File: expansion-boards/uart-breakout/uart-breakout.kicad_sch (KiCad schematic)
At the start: 78 parts, among them J1 Conn_01x06, J2 Conn_01x06, J3 Conn_02x12_Odd_Even, J4 Conn_01x06, J5 Conn_01x06, J6 Conn_01x06, J7 Conn_01x06, J8 Conn_01x06, J9 Conn_01x06, U1 74HC02, U2 74HC00, U3 16C2552_PLCC, U4 DS1813, U5 74LS573, U6 16C2552_PLCC, U7 16C2552_PLCC, U8 16C2552_PLCC, X1 14.7456M

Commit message: [exp-uart] Pre-ERC schematic complete
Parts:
- removed C1: 150u, Capacitor_THT:C_Radial_D8.0mm_H7.0mm_P3.50mm, symbol Device:C_Polarized
- removed R11, R13, R14, R15, R16, R17, R19, R2, R20, R21, R24, R25, R26, R27, R28, R29, R3, R30, R31, R34, R35, R36, R37, R38, R39, R4, R40, R41, R5, R6, R8, R9: 1k, Resistor_THT:R_Axial_DIN0207_L6.3mm_D2.5mm_P7.62mm_Horizontal, symbol Device:R
- removed U1: 74HC02, Package_DIP:DIP-14_W7.62mm, symbol 74xx:74HC02
- removed U5: 74LS573, Package_DIP:DIP-20_W7.62mm, symbol 74xx:74LS573
- added C1, C10, C2, C3, C4, C5, C6, C7, C9: 0.1u, Capacitor_THT:C_Disc_D4.3mm_W1.9mm_P5.00mm, symbol Device:C
- added J10: Conn_01x07, symbol Connector_Generic:Conn_01x07
- added J11: Conn_01x01, symbol Connector_Generic:Conn_01x01
- added J12: Conn_02x12_Odd_Even, Connector_PinSocket_2.54mm:PinSocket_2x12_P2.54mm_Vertical, symbol Connector_Generic:Conn_02x12_Odd_Even
- added R10, R44, R45, R46: 10k, Resistor_THT:R_Axial_DIN0207_L6.3mm_D2.5mm_P7.62mm_Horizontal, symbol Device:R
- added RN1: 1k, Resistor_THT:R_Array_SIP9, symbol Device:R_Network08
- added RN2, RN3, RN4, RN5: 10k, Resistor_THT:R_Array_SIP9, symbol Device:R_Network08
- added SW1: SW_Push, Button_Switch_THT:SW_PUSH_6mm, symbol Switch:SW_Push
- added U1: 74HC04, symbol 74xx:74HC04
- added U10: 74LVC1G07, Package_TO_SOT_SMD:SOT-353_SC-70-5_Handsoldering, symbol 74xGxx:74LVC1G07
- added unit 5 of U2
- added unit 3 of U2
- added U5: 74ACT563, symbol Custom:74ACT563
- added U9: 74HCT164, symbol 74xx:74HCT164
- R18: value 1k -> 10k
- U4: footprint (none) -> Package_TO_SOT_THT:TO-92L_Wide
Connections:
- net A0: now also J12.6 (Pin_6)
- net A1: now also J12.4 (Pin_4)
- net A2: now also J12.5 (Pin_5)
- net A3: now also J12.3 (Pin_3)
- net AUXCSB0: now also U5.1 (OE)
- net AUXCSB1: now also U1.5, U9.2 (DSB)
- net AUXCSB2: now also J12.11 (Pin_11)
- net AUXCSB3: now also J12.13 (Pin_13)
- net B4: now also J12.7 (Pin_7), RN1.5 (R4), U5.16 (Q3)
- net B5: now also RN1.4 (R3), U5.17 (Q2)
- net B6: now also RN1.3 (R2), U5.18 (Q1)
- net B7: now also RN1.2 (R1), U5.19 (Q0)
- net D0: now also J12.8 (Pin_8), U5.9 (D7)
- net D1: now also J12.10 (Pin_10), U5.8 (D6)
- net D2: now also J12.12 (Pin_12), U5.7 (D5)
- net D3: now also J12.14 (Pin_14), U5.6 (D4)
- net D4: now also J12.16 (Pin_16), U5.5 (D3)
- net D5: now also J12.18 (Pin_18), U5.4 (D2)
- net D6: now also J12.20 (Pin_20), U5.3 (D1)
- net D7: now also J12.22 (Pin_22), U5.2 (D0)
- net GND: now also C8.2, C1.2, C10.2, C2.2, C3.2, C4.2, C5.2, C6.2, C7.2, C9.2, J12.23 (Pin_23), J12.24 (Pin_24), R45.2, R46.2, SW1.1, U1.7 (GND), U10.3 (GND), U2.7 (GND), U5.10 (GND), U9.7 (GND); no longer R1.2
- net PHI1: now also U1.2, U5.11 (Load)
- net PHI2: now also U2.2, J12.15 (Pin_15), U1.1, U9.8 (CP)
- net RES: now also U8.21 (RESET), U1.4
- net VDD: now also C8.1, R1.1, C1.1, C10.1, C2.1, C3.1, C4.1, C5.1, C6.1, C7.1, C9.1, J12.1 (Pin_1), R10.1, R44.1, RN1.1 (common), RN2.1 (common), RN3.1 (common), RN4.1 (common), RN5.1 (common), U1.14 (VCC), U10.5 (VCC), U2.14 (VCC), U5.20 (VCC), U9.14 (VCC)
- net /RDB: now also J12.19 (Pin_19)
- net /RDY: now also J12.2 (Pin_2), U10.4
- net /RWB: now also J12.17 (Pin_17)
- net /WRB: now also J12.21 (Pin_21)
- net ~{CD0B}: now also RN2.6 (R5)
- net ~{CD1B}: now also RN2.2 (R1)
- net ~{CD2B}: now also RN3.6 (R5)
- net ~{CD3B}: now also RN3.2 (R1)
- net ~{CD4B}: now also RN4.6 (R5)
- net ~{CD5B}: now also RN4.2 (R1)
- net ~{CD6B}: now also RN5.6 (R5)
- net ~{CD7B}: now also RN5.2 (R1)
- net ~{CS0}: now also RN1.9 (R8), U5.12 (Q7)
- net ~{CS1}: now also RN1.8 (R7), U5.13 (Q6)
- net ~{CS2}: now also RN1.7 (R6), U5.14 (Q5)
- net ~{CS3}: now also RN1.6 (R5), U5.15 (Q4)
- net ~{CTS0B}: now also RN2.7 (R6)
- net ~{CTS1B}: now also RN2.3 (R2)
- net ~{CTS2B}: now also RN3.7 (R6)
- net ~{CTS3B}: now also RN3.3 (R2)
- net ~{CTS4B}: now also RN4.7 (R6)
- net ~{CTS5B}: now also RN4.3 (R2)
- net ~{CTS6B}: now also RN5.7 (R6)
- net ~{CTS7B}: now also RN5.3 (R2)
- net ~{DSR0B}: now also RN2.8 (R7)
- net ~{DSR1B}: now also RN2.4 (R3)
- net ~{DSR2B}: now also RN3.8 (R7)
- net ~{DSR3B}: now also RN3.4 (R3)
- net ~{DSR4B}: now also RN4.8 (R7)
- net ~{DSR5B}: now also RN4.4 (R3)
- net ~{DSR6B}: now also RN5.8 (R7)
- net ~{DSR7B}: now also RN5.4 (R3)
- net ~{RI0B}: now also RN2.9 (R8)
- net ~{RI1B}: now also RN2.5 (R4)
- net ~{RI2B}: now also RN3.9 (R8)
- net ~{RI3B}: now also RN3.5 (R4)
- net ~{RI4B}: now also RN4.9 (R8)
- net ~{RI5B}: now also RN4.5 (R4)
- net ~{RI6B}: now also RN5.9 (R8)
- net ~{RI7B}: now also RN5.5 (R4)
- net at U2.4: now also R18.1
- net at U2.5: now also R46.1
- net at U4.1 (RST): now also R1.2, SW1.2, U1.3
- net at U2.11: now also U10.2, U2.10
- net at U2.12: now also U1.8
- net at U2.13: now also J11.1 (Pin_1)
- net at U2.1: now also U1.6
- net CSB_CLOCKED: now reaches U2.3
- net CSB_CLOCKED: now also U2.9
- new net: R44.2, U9.1 (DSA)
- new net: U1.11, U2.8
- new net: J10.1 (Pin_1), U9.4 (Q1)
- new net: J10.2 (Pin_2), U9.5 (Q2)
- new net: J10.3 (Pin_3), U9.6 (Q3)
- new net: J10.4 (Pin_4), U9.10 (Q4)
- new net: J10.5 (Pin_5), U9.11 (Q5)
- new net: J10.6 (Pin_6), U9.12 (Q6)
- new net: J10.7 (Pin_7), U9.13 (Q7)
- new net: R10.2, U9.9 (~{MR})
- new net: R45.1, U1.13
- new net: U1.9, U9.3 (Q0)
- new net CSB_SLOW: J12.9 (Pin_9), U1.10
- no-connect marks 33 -> 32
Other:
- note added: "RESET"
- moved on the sheet: C11, C8, H1, H2, H3, H4, H5, H6, J3, R18, U2A, U2B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

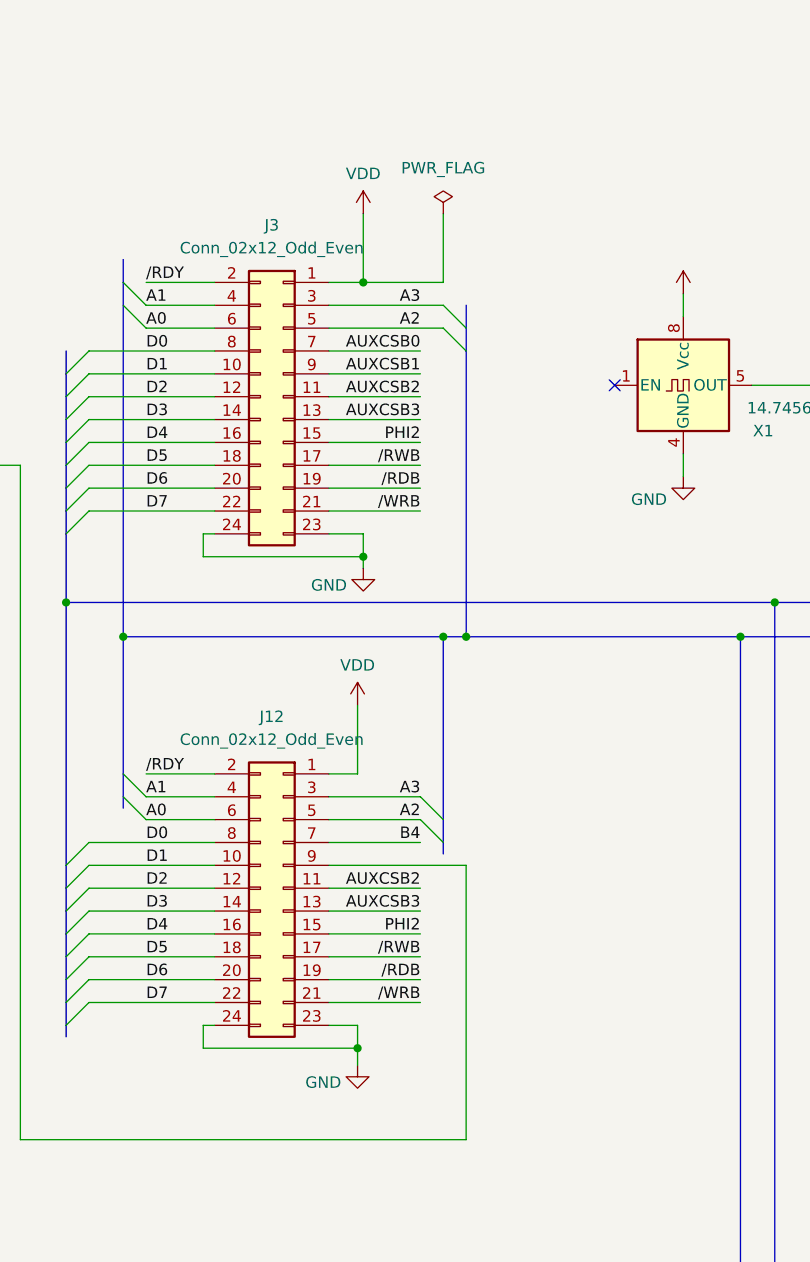
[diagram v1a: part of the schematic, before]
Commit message: [exp-uart] Pass ERC
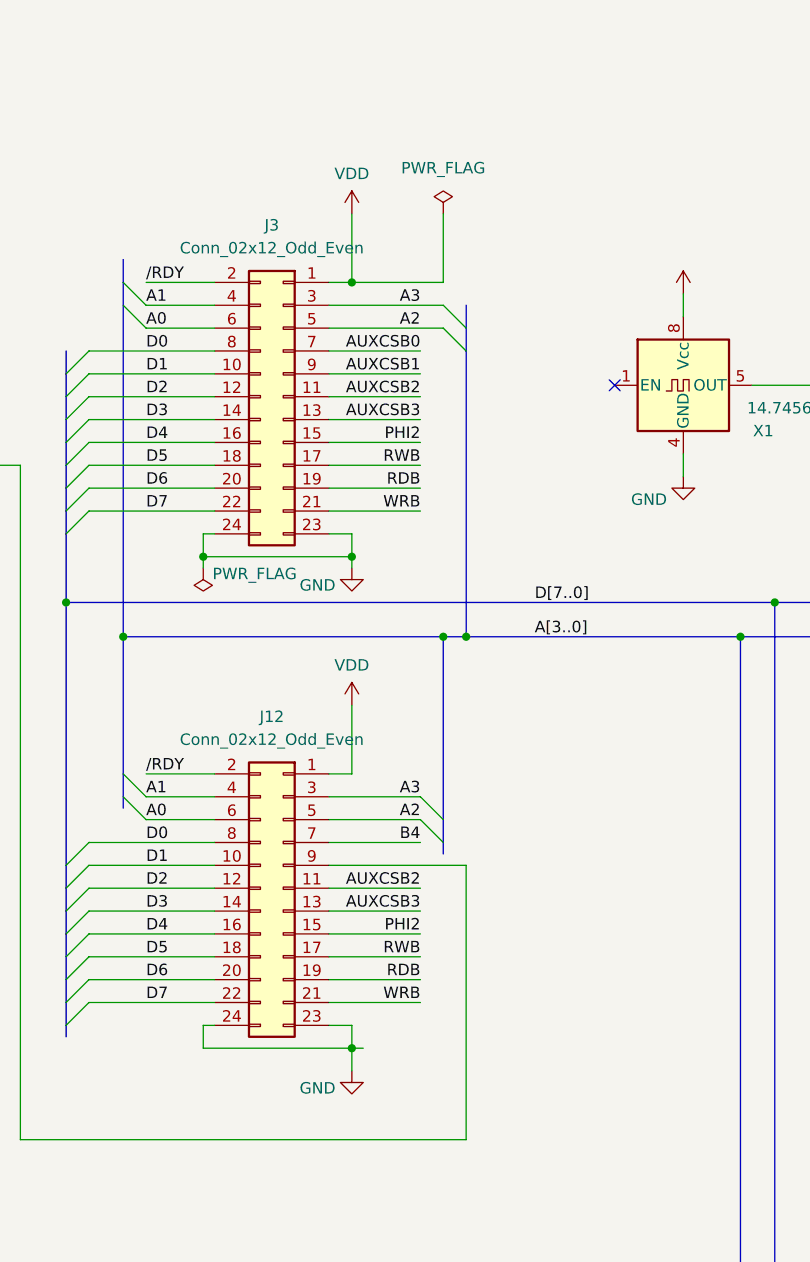
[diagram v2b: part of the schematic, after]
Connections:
- net /RDB is gone; now on net RDB: J12.19 (Pin_19), J3.19 (Pin_19)
- net /WRB is gone; now on net WRB: J12.21 (Pin_21), J3.21 (Pin_21)
- net /RWB renamed RWB

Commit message: [exp-uart] Reannotate & footprint assignment
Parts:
- added J1: Conn_01x03, Connector_PinSocket_2.54mm:PinSocket_1x03_P2.54mm_Vertical, symbol Connector_Generic:Conn_01x03
- J10: renamed from J6; footprint (none) -> Connector_PinSocket_2.54mm:PinSocket_1x06_P2.54mm_Vertical
- J11: renamed from J8; footprint (none) -> Connector_PinSocket_2.54mm:PinSocket_1x06_P2.54mm_Vertical
- J12: renamed from J7; footprint (none) -> Connector_PinSocket_2.54mm:PinSocket_1x06_P2.54mm_Vertical
- J13: renamed from J9; footprint (none) -> Connector_PinSocket_2.54mm:PinSocket_1x06_P2.54mm_Vertical
- J2: renamed from J1; footprint (none) -> Connector_PinSocket_2.54mm:PinSocket_1x06_P2.54mm_Vertical
- J3: renamed from J4; footprint (none) -> Connector_PinSocket_2.54mm:PinSocket_1x06_P2.54mm_Vertical
- J5: renamed from J2; footprint (none) -> Connector_PinSocket_2.54mm:PinSocket_1x06_P2.54mm_Vertical
- J6: renamed from J5; footprint (none) -> Connector_PinSocket_2.54mm:PinSocket_1x06_P2.54mm_Vertical
- J7: renamed from J11; footprint (none) -> Connector_PinSocket_2.54mm:PinSocket_1x01_P2.54mm_Vertical
- J8: renamed from J10; footprint (none) -> Connector_PinSocket_2.54mm:PinSocket_1x07_P2.54mm_Vertical
- U2: renamed from U1; footprint (none) -> Package_DIP:DIP-14_W7.62mm
- U3: renamed from U5; footprint (none) -> Package_DIP:DIP-20_W7.62mm
- U7: renamed from U9; footprint (none) -> Package_DIP:DIP-14_W7.62mm
- renumbered C11 to C1, C9 to C10, C10 to C11, C8 to C2, C1 to C3, C2 to C4, C3 to C5, C4 to C6, C5 to C7, C6 to C8, C7 to C9, D4 to D2, D5 to D4, D6 to D5, D8 to D6, D9 to D8, H3 to H1, H5 to H2, H2 to H3, H6 to H5, H1 to H6, J3 to J4, J12 to J9, R33 to R10, R43 to R11, R45 to R12, R18 to R13, R46 to R14, R7 to R2, R22 to R3, R12 to R4, R23 to R5, R44 to R6, R10 to R7, R32 to R8, R42 to R9, U4 to U1, U8 to U10, U3 to U4, U6 to U5, U2 to U6, U10 to U8, U7 to U9
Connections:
- net B5: now also J1.3 (Pin_3)
- net B6: now also J1.2 (Pin_2)
- net B7: now also J1.1 (Pin_1)
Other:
- note added: "Jumper sets number of wait cycles (min. 1)"

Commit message: [exp-uart] Remove most UART LEDs; Initial pcb placement
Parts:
- removed C8, C9: 0.1u, Capacitor_THT:C_Disc_D4.3mm_W1.9mm_P5.00mm, symbol Device:C
- removed D2, D3, D4, D5, D6, D7, D8: LED, LED_THT:LED_D5.0mm, symbol Device:LED
- removed R10, R11, R3, R4, R5, R8, R9: 330, Resistor_THT:R_Axial_DIN0207_L6.3mm_D2.5mm_P7.62mm_Horizontal, symbol Device:R
- renumbered C10 to C8, C11 to C9, R6 to R3, R7 to R4, R12 to R5, R13 to R6, R14 to R7
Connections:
- net ~{MF0B}: now also D1.2 (A)
- net ~{MF1B}: no longer D1.2 (A)
- no-connect marks 32 -> 39
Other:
- moved on the sheet: C8, C9, D1, R2

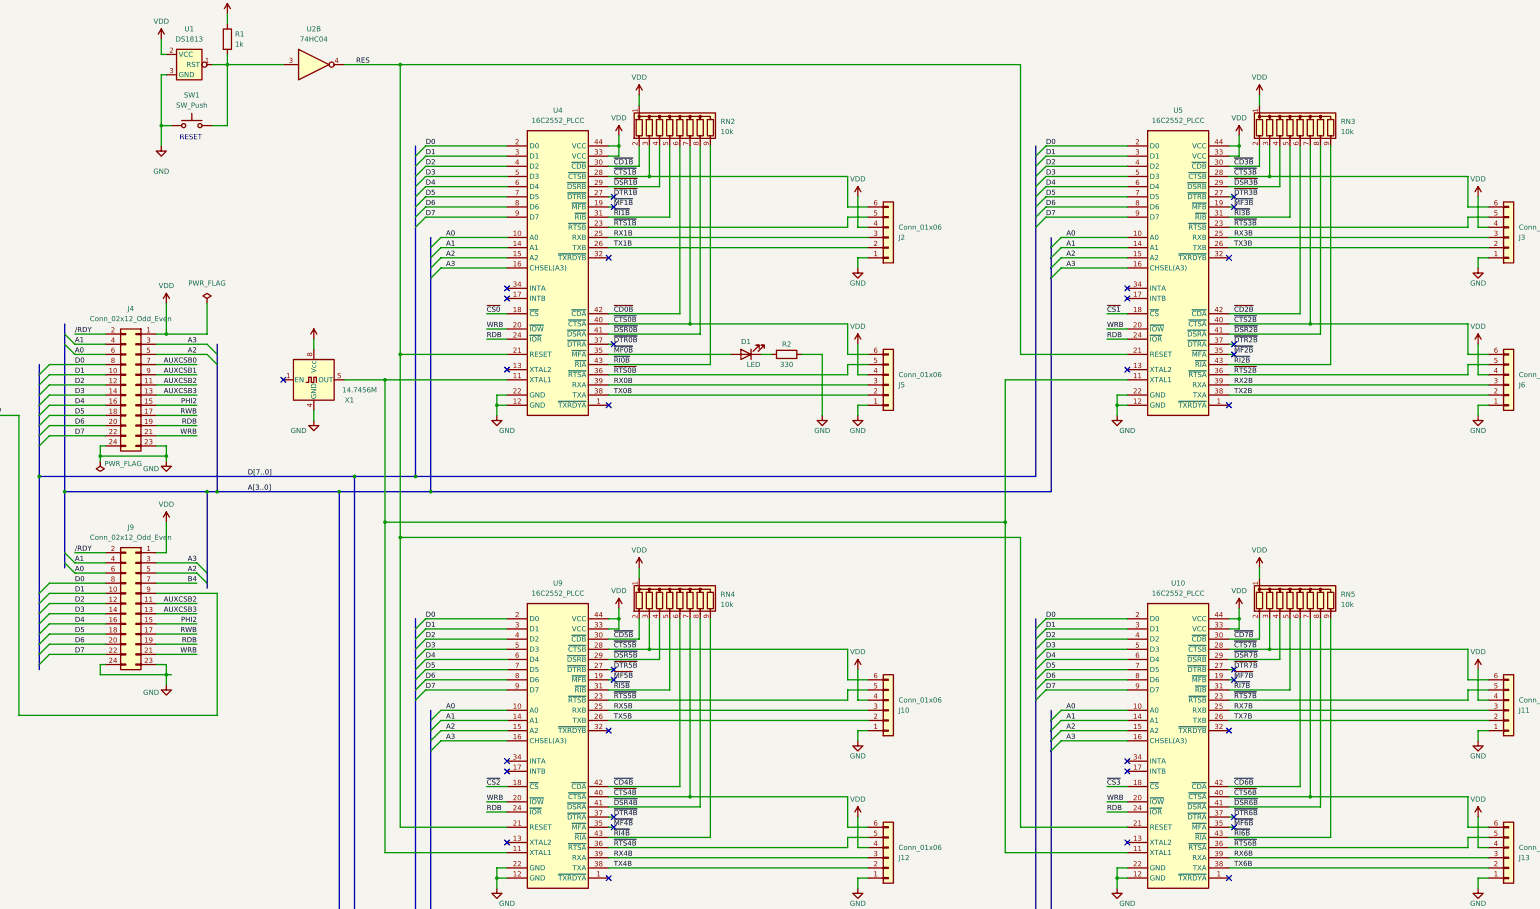
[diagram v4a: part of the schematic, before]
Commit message: [exp-uart] 90% routed
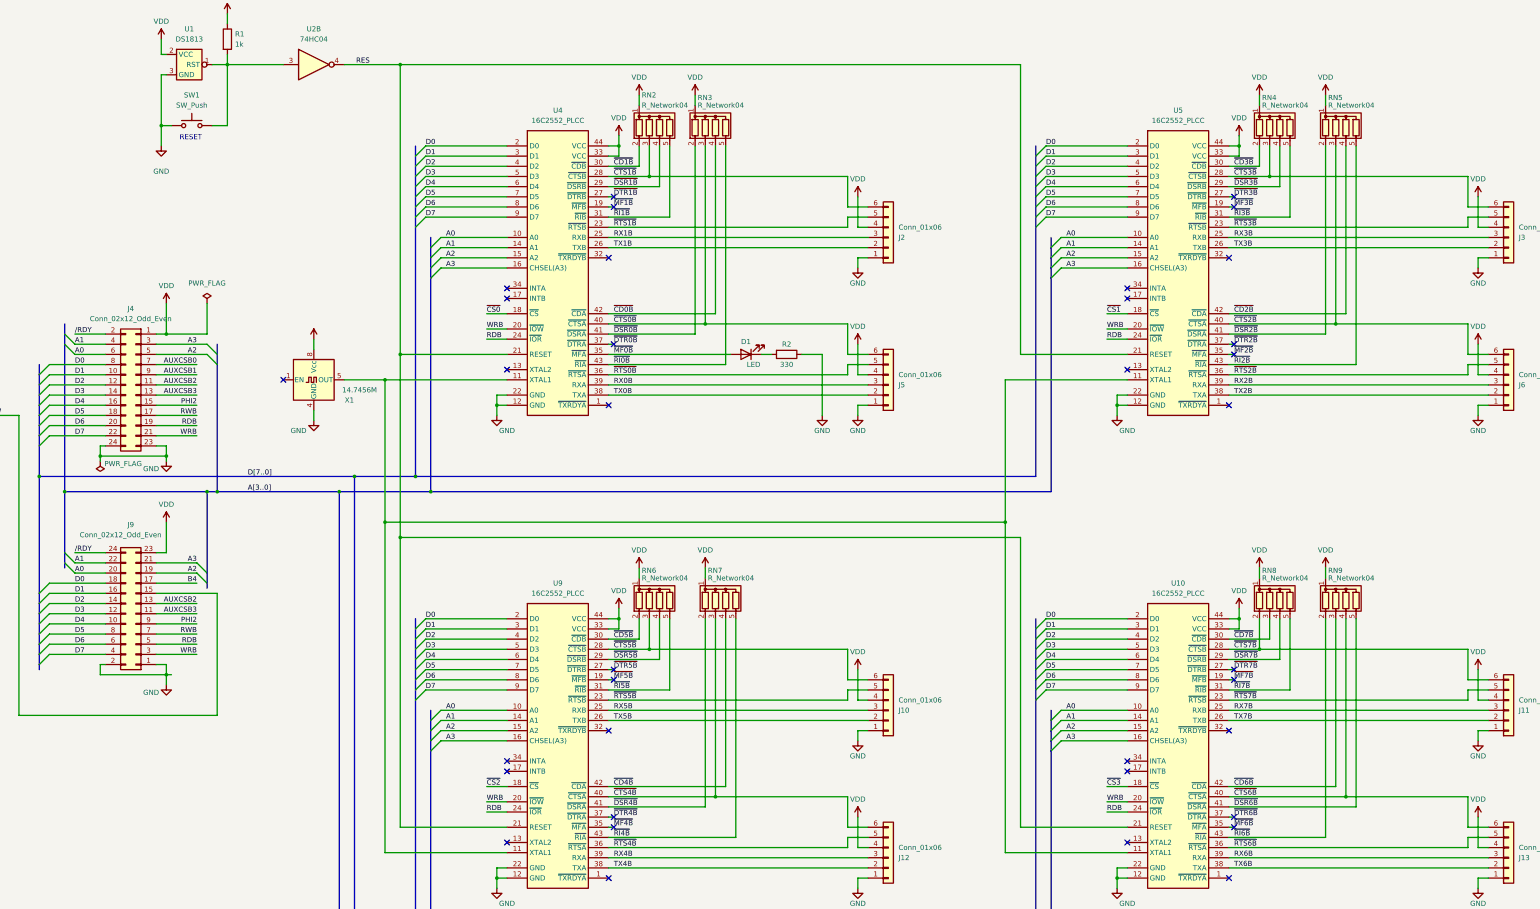
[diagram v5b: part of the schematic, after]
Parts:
- removed RN2, RN3, RN4, RN5: 10k, Resistor_THT:R_Array_SIP9, symbol Device:R_Network08
- added RN2, RN3, RN4, RN5, RN6, RN7, RN8, RN9: R_Network04, Resistor_THT:R_Array_SIP5, symbol Device:R_Network04
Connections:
- net A0: now also J9.20 (Pin_20); no longer J9.6 (Pin_6)
- net A1: now also J9.22 (Pin_22); no longer J9.4 (Pin_4)
- net A2: now also J9.19 (Pin_19); no longer J9.5 (Pin_5)
- net A3: now also J9.21 (Pin_21); no longer J9.3 (Pin_3)
- net AUXCSB2: now also J9.13 (Pin_13); no longer J9.11 (Pin_11)
- net AUXCSB3: now also J9.11 (Pin_11); no longer J9.13 (Pin_13)
- net B4: now also J9.17 (Pin_17); no longer J9.7 (Pin_7)
- net CSB_SLOW: now also J9.15 (Pin_15); no longer J9.9 (Pin_9)
- net D0: now also J9.18 (Pin_18); no longer J9.8 (Pin_8)
- net D1: now also J9.16 (Pin_16); no longer J9.10 (Pin_10)
- net D2: now also J9.14 (Pin_14); no longer J9.12 (Pin_12)
- net D3: now also J9.12 (Pin_12); no longer J9.14 (Pin_14)
- net D4: now also J9.10 (Pin_10); no longer J9.16 (Pin_16)
- net D5: now also J9.8 (Pin_8); no longer J9.18 (Pin_18)
- net D6: now also J9.6 (Pin_6); no longer J9.20 (Pin_20)
- net D7: now also J9.4 (Pin_4); no longer J9.22 (Pin_22)
- net GND: now also J9.1 (Pin_1), J9.2 (Pin_2); no longer J9.23 (Pin_23), J9.24 (Pin_24)
- net PHI2: now also J9.9 (Pin_9); no longer J9.15 (Pin_15)
- net RDB: now also J9.5 (Pin_5); no longer J9.19 (Pin_19)
- net RWB: now also J9.7 (Pin_7); no longer J9.17 (Pin_17)
- net VDD: now also J9.23 (Pin_23), RN2.1 (common), RN3.1 (common), RN4.1 (common), RN5.1 (common), RN6.1 (common), RN7.1 (common), RN8.1 (common), RN9.1 (common); no longer J9.1 (Pin_1)
- net WRB: now also J9.3 (Pin_3); no longer J9.21 (Pin_21)
- net /RDY: now also J9.24 (Pin_24); no longer J9.2 (Pin_2)
- net ~{CD0B}: now also RN3.4 (R3)
- net ~{CD1B}: now also RN2.2 (R1)
- net ~{CD2B}: now also RN5.4 (R3)
- net ~{CD3B}: now also RN4.2 (R1)
- net ~{CD4B}: now also RN7.4 (R3)
- net ~{CD5B}: now also RN6.2 (R1)
- net ~{CD6B}: now also RN9.3 (R2)
- net ~{CD7B}: now also RN8.3 (R2)
- net ~{CTS0B}: now also RN3.3 (R2)
- net ~{CTS1B}: now also RN2.3 (R2)
- net ~{CTS2B}: now also RN5.3 (R2)
- net ~{CTS3B}: now also RN4.3 (R2)
- net ~{CTS4B}: now also RN7.3 (R2)
- net ~{CTS5B}: now also RN6.3 (R2)
- net ~{CTS6B}: now also RN9.4 (R3)
- net ~{CTS7B}: now also RN8.2 (R1)
- net ~{DSR0B}: now also RN3.2 (R1)
- net ~{DSR1B}: now also RN2.4 (R3)
- net ~{DSR2B}: now also RN5.2 (R1)
- net ~{DSR3B}: now also RN4.4 (R3)
- net ~{DSR4B}: now also RN7.2 (R1)
- net ~{DSR5B}: now also RN6.4 (R3)
- net ~{DSR6B}: now also RN9.5 (R4)
- net ~{DSR7B}: now also RN8.4 (R3)
- net ~{RI0B}: now also RN3.5 (R4)
- net ~{RI1B}: now also RN2.5 (R4)
- net ~{RI2B}: now also RN5.5 (R4)
- net ~{RI3B}: now also RN4.5 (R4)
- net ~{RI4B}: now also RN7.5 (R4)
- net ~{RI5B}: now also RN6.5 (R4)
- net ~{RI6B}: now also RN9.2 (R1)
- net ~{RI7B}: now also RN8.5 (R4)
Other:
- moved on the sheet: J9

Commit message: [exp-uart] Layout complete; Pass DRC
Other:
- title: ZEDIAC Expansion Card Template -> ZEDIAC Uart Expansion Card
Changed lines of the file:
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@@
 	(paper "User" 599.999 399.999)
 	(title_block
-		(title "ZEDIAC Expansion Card Template")
-		(date "2024-03-10")
+		(title "ZEDIAC Uart Expansion Card")
+		(date "2024-03-16")
 		(rev "1.1")
 		(company "Electronics Tinkerer")
